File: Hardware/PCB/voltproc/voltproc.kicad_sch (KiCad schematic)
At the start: 55 parts, among them J1 Synth_power_2x5, J10 Jack, J11 Jack, J12 Jack, J13 Jack, J2 Jack, J3 Jack, J4 Jack, J5 Jack, J6 Jack, J7 Jack, J8 Jack, J9 Jack, U1 TL074, U2 TL071

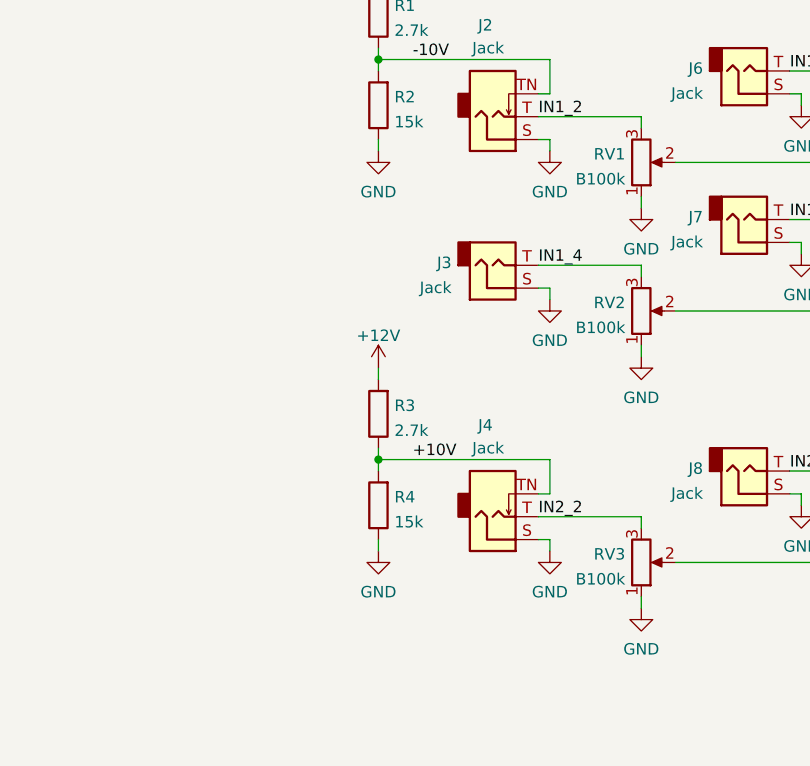
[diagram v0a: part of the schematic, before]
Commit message: normal 2nd pot on 1st section
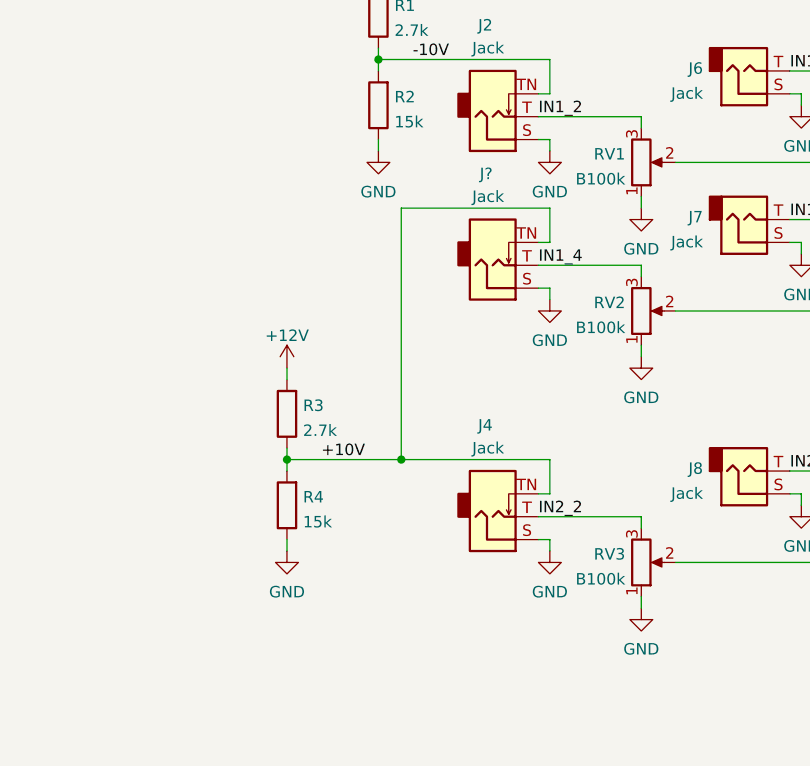
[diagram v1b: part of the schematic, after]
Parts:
- removed J3: Jack, symbol Connector:AudioJack2
- added J?: Jack, symbol Connector:AudioJack2_SwitchT
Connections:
- net +10V: now also J?.TN
- net GND: now also J?.S
- net IN1_4: now also J?.T
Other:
- moved on the sheet: R3, R4
